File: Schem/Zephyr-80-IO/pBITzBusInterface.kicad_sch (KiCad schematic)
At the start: 1 part, among them J1 pBITzBus

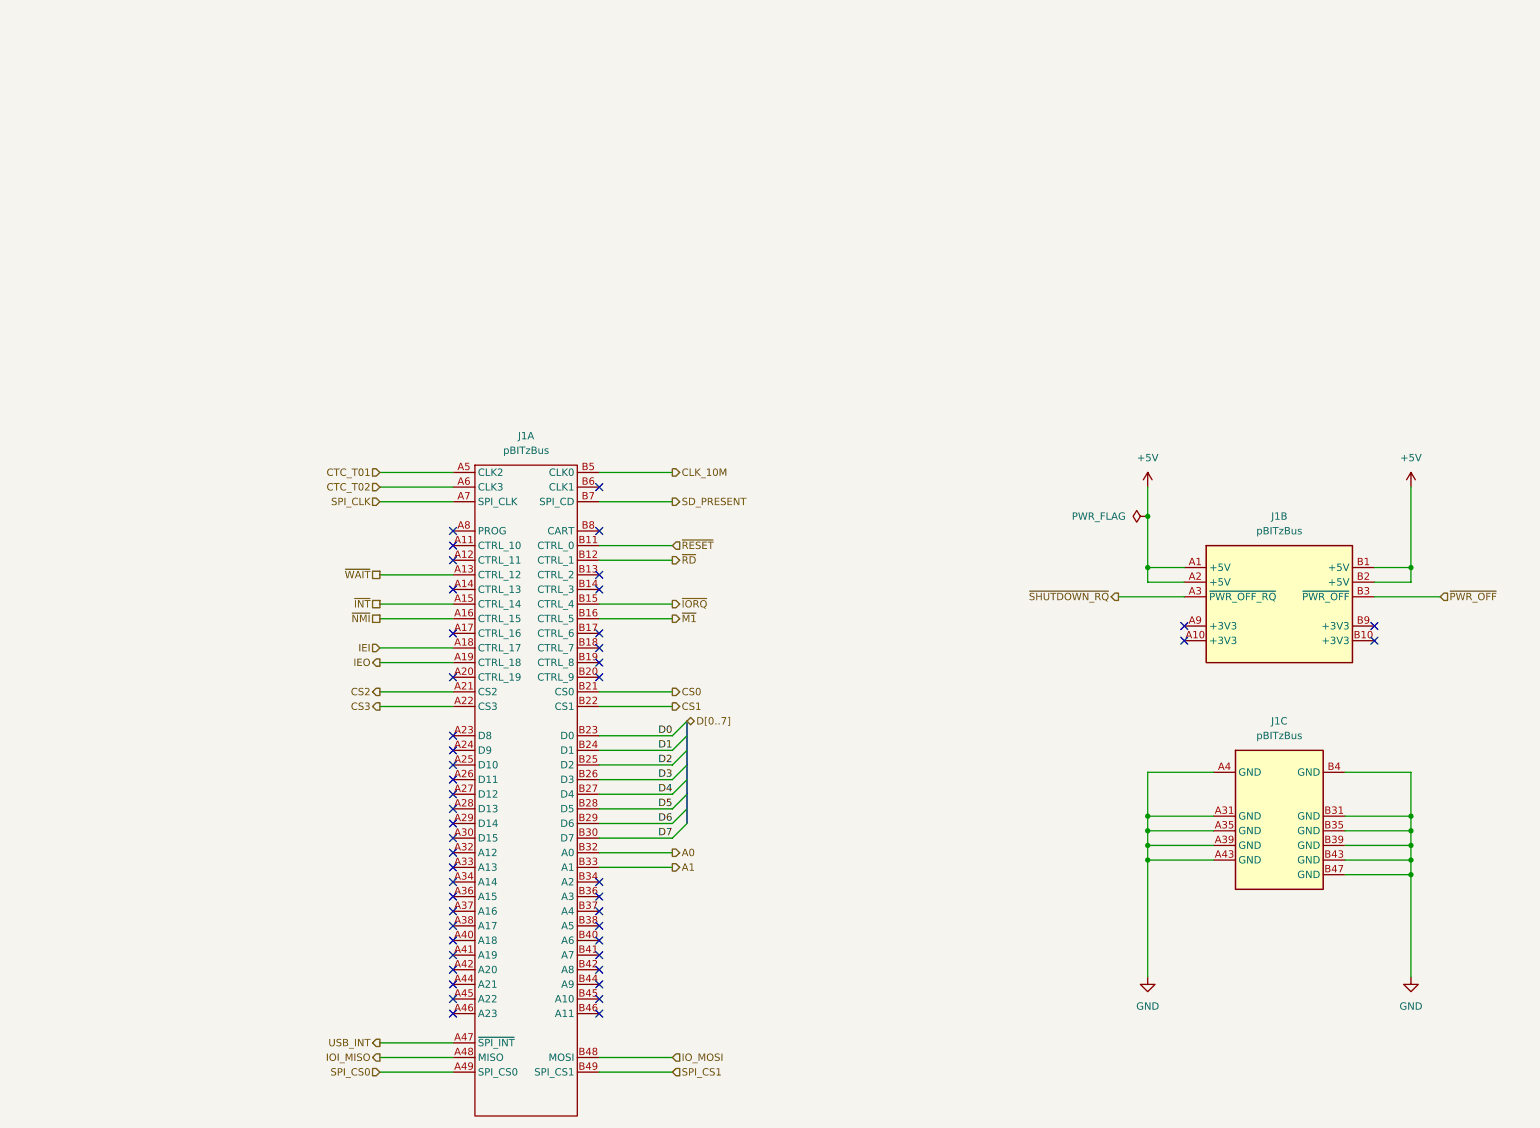
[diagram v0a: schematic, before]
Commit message: Moved to the DIN Connector
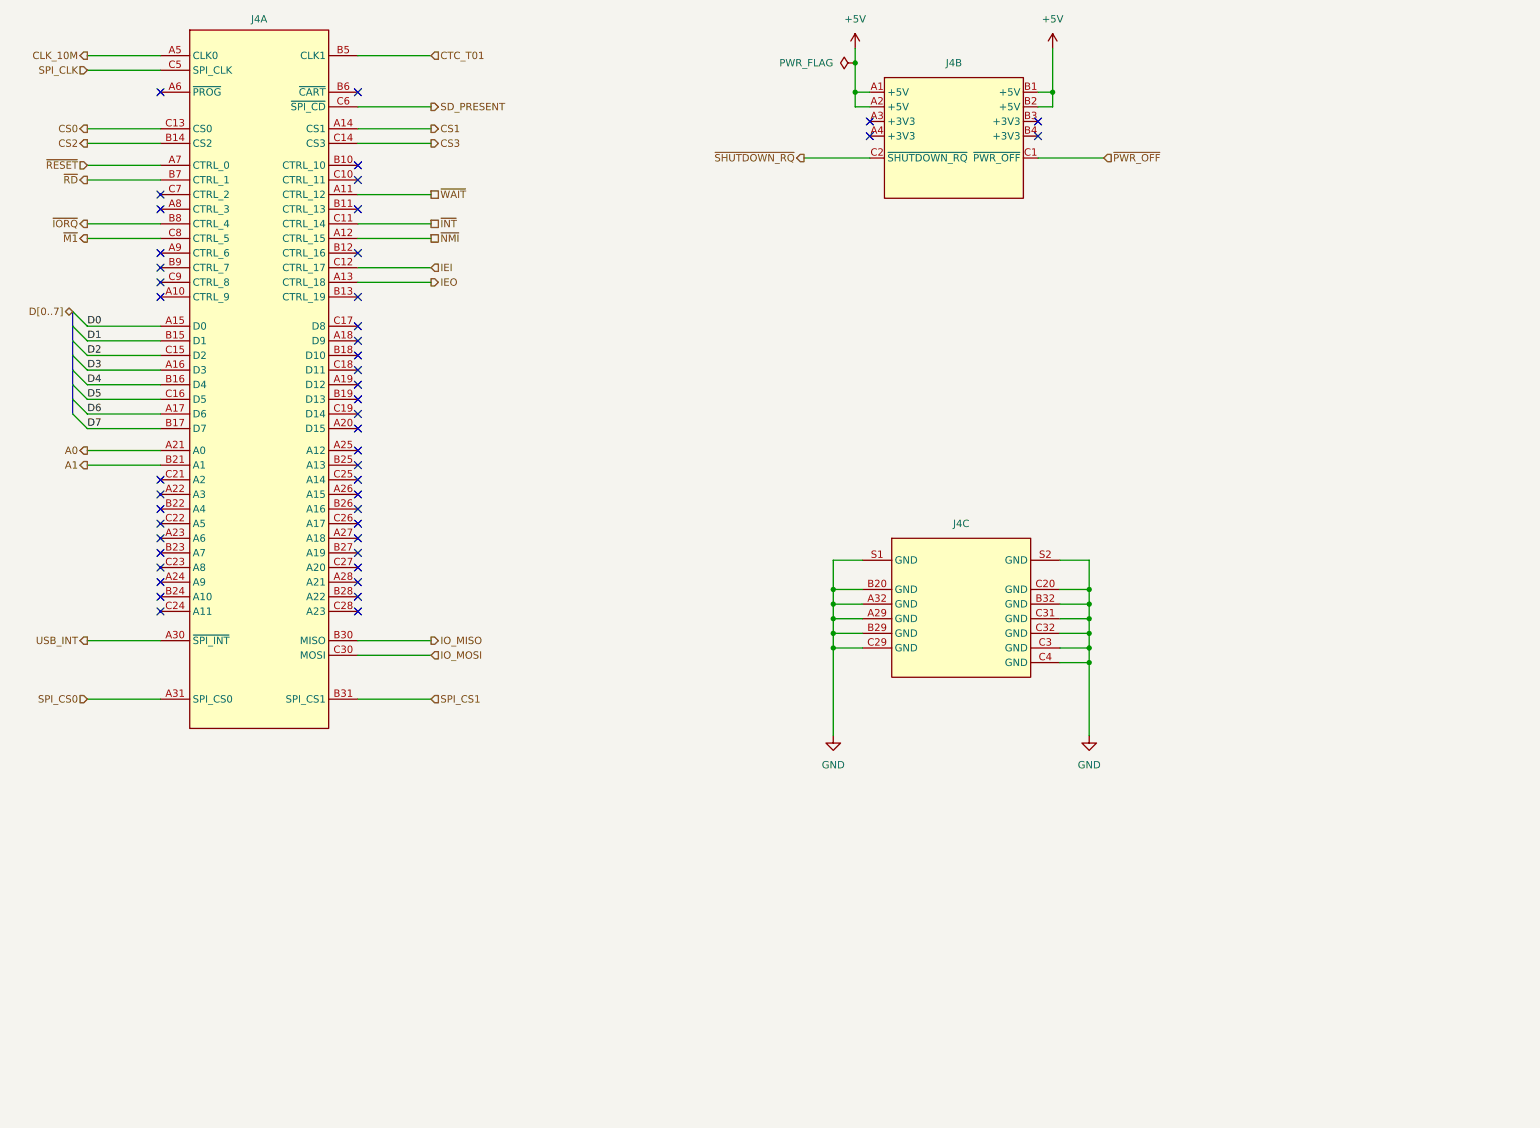
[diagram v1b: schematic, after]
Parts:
- removed J1: pBITzBus, Connector_PCBEdge:BUS_PCIexpress_x8, symbol pBITz:pBITzBus
- added J4: (no value), Footprints:AMPHENOL_86093967113T55F1LF, symbol pBITz:pBITzBus_DIN
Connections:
- net +5V: now also J4.A1 (+5V), J4.A2 (+5V), J4.B1 (+5V), J4.B2 (+5V)
- net A0: now also J4.A21 (A0)
- net A1: now also J4.B21 (A1)
- net CLK_10M: now also J4.A5 (CLK0)
- net CS0: now also J4.C13 (CS0)
- net CS1: now also J4.A14 (CS1)
- net CS2: now also J4.B14 (CS2)
- net CS3: now also J4.C14 (CS3)
- net CTC_T01: now also J4.B5 (CLK1)
- net D0: now also J4.A15 (D0)
- net D1: now also J4.B15 (D1)
- net D2: now also J4.C15 (D2)
- net D3: now also J4.A16 (D3)
- net D4: now also J4.B16 (D4)
- net D5: now also J4.C16 (D5)
- net D6: now also J4.A17 (D6)
- net D7: now also J4.B17 (D7)
- net GND: now also J4.A29 (GND), J4.A32 (GND), J4.B20 (GND), J4.B29 (GND), J4.B32 (GND), J4.C20 (GND), J4.C29 (GND), J4.C3 (GND), J4.C31 (GND), J4.C32 (GND), J4.C4 (GND), J4.S1 (GND), J4.S2 (GND)
- net IEI: now also J4.C12 (CTRL_17)
- net IEO: now also J4.A13 (CTRL_18)
- net IO_MOSI: now also J4.C30 (MOSI)
- net SD_PRESENT: now also J4.C6 (~{SPI_CD})
- net SPI_CLK: now also J4.C5 (SPI_CLK)
- net SPI_CS0: now also J4.A31 (SPI_CS0)
- net SPI_CS1: now also J4.B31 (SPI_CS1)
- net USB_INT: now also J4.A30 (~{SPI_INT})
- net ~{INT}: now also J4.C11 (CTRL_14)
- net ~{IORQ}: now also J4.B8 (CTRL_4)
- net ~{M1}: now also J4.C8 (CTRL_5)
- net ~{NMI}: now also J4.A12 (CTRL_15)
- net ~{PWR_OFF}: now also J4.C1 (~{PWR_OFF})
- net ~{RD}: now also J4.B7 (CTRL_1)
- net ~{RESET}: now also J4.A7 (CTRL_0)
- net ~{SHUTDOWN_RQ}: now also J4.C2 (~{SHUTDOWN_RQ})
- net ~{WAIT}: now also J4.A11 (CTRL_12)
- new net IO_MISO: J4.B30 (MISO)
- no-connect marks 48 -> 47

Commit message: updated parts #s
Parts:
- J4: MANUFACTURER_PART_NUMBER AMPHENOL_86093967113T55F1LF -> 86093967113T55F1LF
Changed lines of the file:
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@@
 			)
 		)
-		(property "MANUFACTURER_PART_NUMBER" "AMPHENOL_86093967113T55F1LF"
+		(property "MANUFACTURER_PART_NUMBER" "86093967113T55F1LF"
 			(at 196.215 134.62 0)
 			(hide yes)
@@
 			)
 		)
-		(property "MANUFACTURER_PART_NUMBER" "AMPHENOL_86093967113T55F1LF"
+		(property "MANUFACTURER_PART_NUMBER" "86093967113T55F1LF"
 			(at 74.295 46.99 0)
 			(hide yes)
@@
 			)
 		)
-		(property "MANUFACTURER_PART_NUMBER" "AMPHENOL_86093967113T55F1LF"
+		(property "MANUFACTURER_PART_NUMBER" "86093967113T55F1LF"
 			(at 194.945 55.88 0)
 			(hide yes)
